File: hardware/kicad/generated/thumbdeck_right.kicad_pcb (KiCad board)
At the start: 2 copper layers, 63 x 107.9 mm, 0 parts

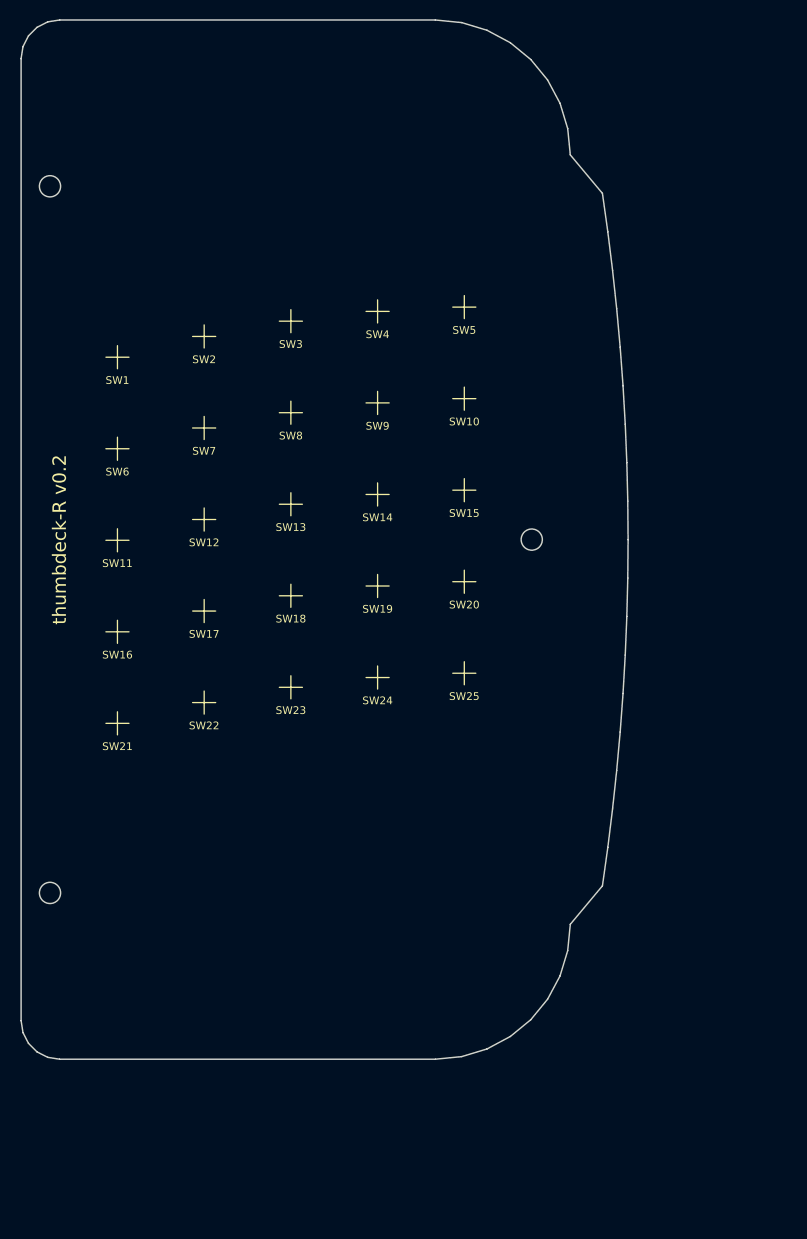
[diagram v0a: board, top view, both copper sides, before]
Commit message: hardware(v0.3): role-based geometry, grader, board gen
- deck.py: right grip = mcu (nice!nano/LiPo/USB-C/bridge), left = passive matrix
  + bridge connector; symmetric outline, mirrored key field
- grade.py: 17 checks incl. F-bridge + F-role; nice!nano pro_micro pin validity;
  single 5x10 transform (dropped split-specific checks)
- gen_kicad/render_fab/matrix_map updated for single controller

Co-Authored-By: Claude Opus 4.8 (1M context) <noreply@anthropic.com>
Claude-Session: https://claude.ai/code/session_01AmPvvwwHX98PjdDnPxhX97
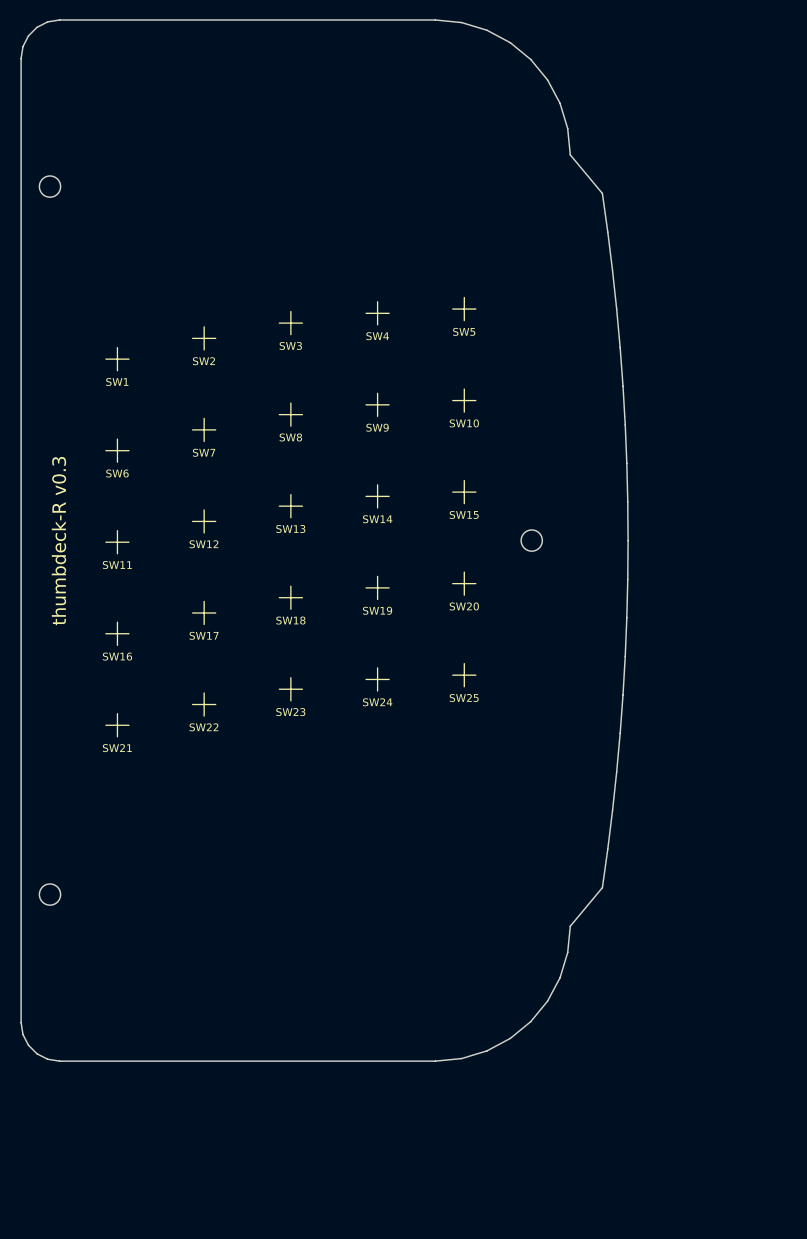
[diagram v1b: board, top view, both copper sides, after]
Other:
- board size 63 x 107.9 mm -> 63 x 108.1 mm
- board text added: "BRIDGE"
- board text added: "thumbdeck-R v0.3"
- board text removed: "thumbdeck-R v0.2"

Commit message: v0.4: encode EE design review into the grade, re-converge to PASS
Turn the professional EE review findings into enforced checks and fix the design
to satisfy them (functional 27/27, visual 9/9, OVERALL PASS).

Geometry/RF:
- nice!nano remounted vertical at top; nRF52840 ANTENNA keep-out overhangs the
  top edge (no copper under RF path), LiPo kept ~90mm away; USB in an access gap
- new hard check F-antenna; F-role now requires antenna on right / passive left

Bridge signal integrity:
- kscan debounce 8ms (F-si-debounce); BOM adds 4.7k row pull-downs, 100-330R
  column series R, TVS, shielded flex (F-si-passives, F-esd-tvs)

Process/plan gates (now graded):
- F-charge (1C vs cell), F-switch-verify (meter pinout), F-review-doc
  (docs/design-review.md + FMEA), F-bringup (current-draw checkpoints),
  F-fab-gates (README gates fab on schematic+ERC+DRC+CI)

Fixes: antenna/controller touching edge tripped float overlap -> 0.6mm gap;
BOM 'series res' substring broke on markdown bold -> looser check.
Bump VERSION v0.3 -> v0.4; regenerate all renders/board/soldermap.

Co-Authored-By: Claude Opus 4.8 (1M context) <noreply@anthropic.com>
Claude-Session: https://claude.ai/code/session_01AmPvvwwHX98PjdDnPxhX97
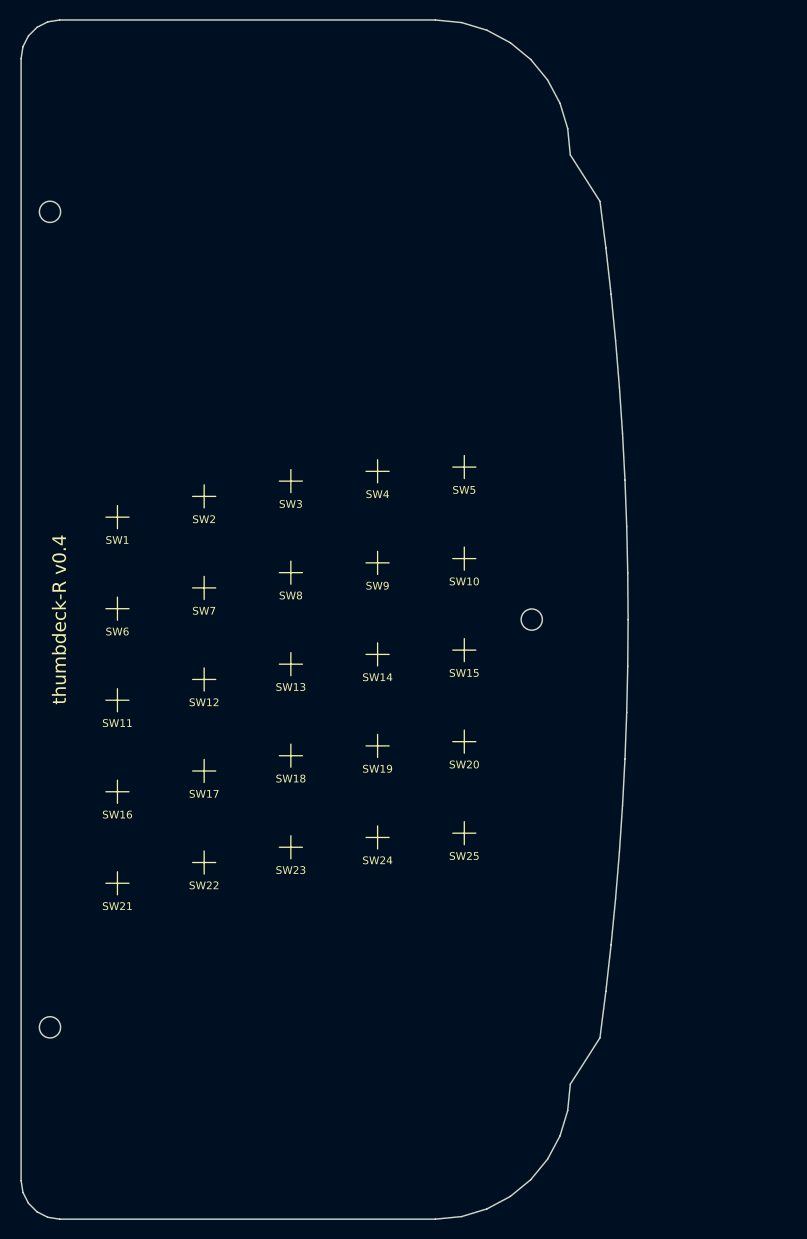
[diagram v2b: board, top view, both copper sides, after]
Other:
- board size 63 x 108.1 mm -> 63 x 124.5 mm
- board text added: "ANTENNA"
- board text added: "thumbdeck-R v0.4"
- board text removed: "thumbdeck-R v0.3"

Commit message: v0.12: snap-dome phone MagSafe deck — module, turnkey PCBA, stackable layer renders
Redesign from v0.4 (50-key nice!nano) to a landscape-phone MagSafe deck:

- Switches: Snaptron 7mm snap domes on a one-piece 3D-printed living-hinge keymat
  (PocketMage-style); footprint extracted to hardware/footprints/. 81 keys (2x 6x6
  grids + D-pad/OK + mouse + PgUp/Dn), digitized from the sketch to
  hardware/layout/keymat.json.
- Form: phone landscape, MagSafe-mounted centre; LiPo in the spine behind the ring;
  two ~70x102mm grips clamped to the outline; PCB-integrated trackpad (Azoteq IQS7211E).
- Electronics (5-lens EE/PD review): one Ebyte E73 nRF52840 module, 9x10 col2row
  matrix with SOD-323 diodes on the back, power front-end (MCP73831/USB-C+CC/ESD),
  vertical JST-GH bridge, ENIG. Layer-correct traces (cols front / rows back / vias),
  PCB meander antenna option.
- Sourcing (JLC vs PCBWay review): JLCPCB single-sided turnkey, ~$150-230/5 sets;
  part swaps + LCSC part numbers in docs/fabrication-sourcing.md.
- Real netlisted KiCad boards via pcbnew (gen_kicad_pcbnew.py) + front/back SVGs.
- 5 stackable layer renders (render_layers.py) + product/fab views; README rewritten.
- Cleanup: old 50-key loop scripts -> hardware/scripts/legacy/; old iters/renders
  -> renders/history/.

Co-Authored-By: Claude Opus 4.8 <noreply@anthropic.com>
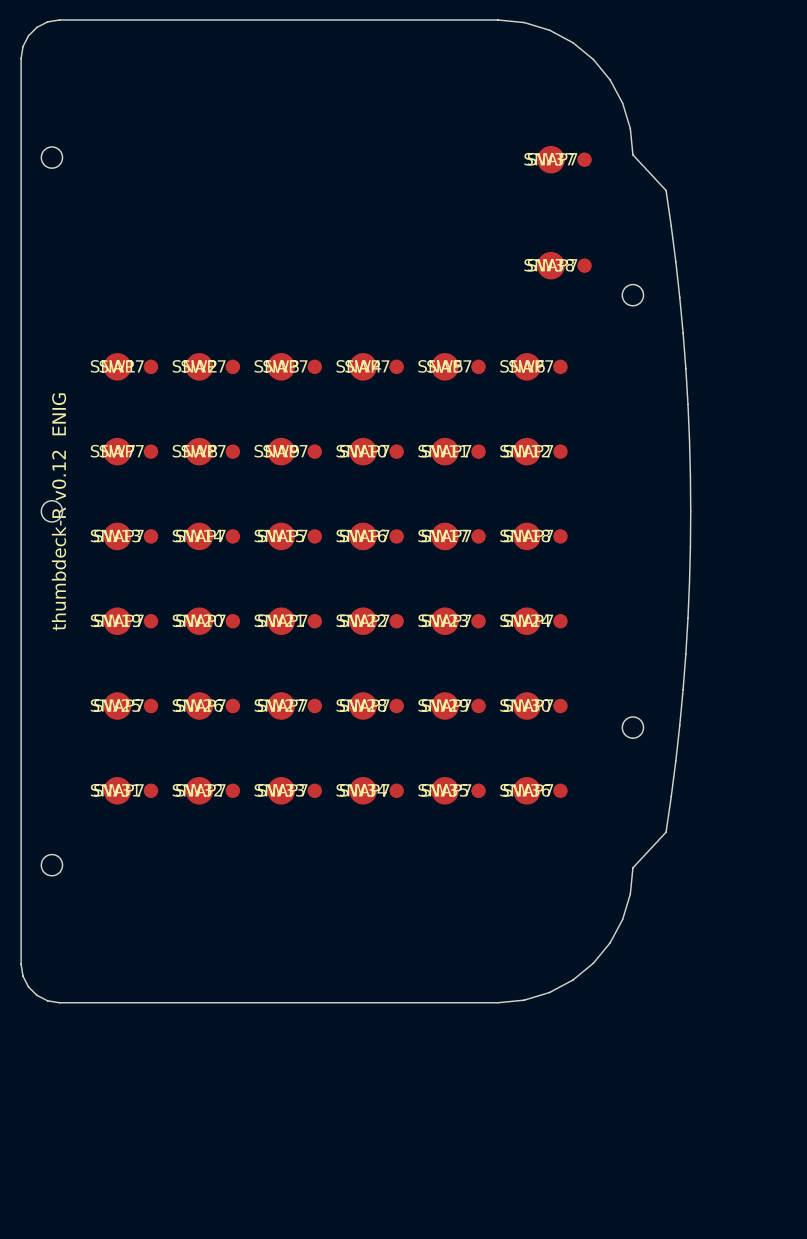
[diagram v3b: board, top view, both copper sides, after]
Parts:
- added D1: 1N4148WS, D_SOD-323, B.Cu at (10.0, 35.8)
- added D10: 1N4148WS, D_SOD-323, B.Cu at (35.5, 44.6)
- added D11: 1N4148WS, D_SOD-323, B.Cu at (44.0, 44.6)
- added D12: 1N4148WS, D_SOD-323, B.Cu at (52.5, 44.6)
- added D13: 1N4148WS, D_SOD-323, B.Cu at (10.0, 53.4)
- added D14: 1N4148WS, D_SOD-323, B.Cu at (18.5, 53.4)
- added D15: 1N4148WS, D_SOD-323, B.Cu at (27.0, 53.4)
- added D16: 1N4148WS, D_SOD-323, B.Cu at (35.5, 53.4)
- added D17: 1N4148WS, D_SOD-323, B.Cu at (44.0, 53.4)
- added D18: 1N4148WS, D_SOD-323, B.Cu at (52.5, 53.4)
- added D19: 1N4148WS, D_SOD-323, B.Cu at (10.0, 62.2)
- added D2: 1N4148WS, D_SOD-323, B.Cu at (18.5, 35.8)
- added D20: 1N4148WS, D_SOD-323, B.Cu at (18.5, 62.2)
- added D21: 1N4148WS, D_SOD-323, B.Cu at (27.0, 62.2)
- added D22: 1N4148WS, D_SOD-323, B.Cu at (35.5, 62.2)
- added D23: 1N4148WS, D_SOD-323, B.Cu at (44.0, 62.2)
- added D24: 1N4148WS, D_SOD-323, B.Cu at (52.5, 62.2)
- added D25: 1N4148WS, D_SOD-323, B.Cu at (10.0, 71.0)
- added D26: 1N4148WS, D_SOD-323, B.Cu at (18.5, 71.0)
- added D27: 1N4148WS, D_SOD-323, B.Cu at (27.0, 71.0)
- added D28: 1N4148WS, D_SOD-323, B.Cu at (35.5, 71.0)
- added D29: 1N4148WS, D_SOD-323, B.Cu at (44.0, 71.0)
- added D3: 1N4148WS, D_SOD-323, B.Cu at (27.0, 35.8)
- added D30: 1N4148WS, D_SOD-323, B.Cu at (52.5, 71.0)
- added D31: 1N4148WS, D_SOD-323, B.Cu at (10.0, 79.8)
- added D32: 1N4148WS, D_SOD-323, B.Cu at (18.5, 79.8)
- added D33: 1N4148WS, D_SOD-323, B.Cu at (27.0, 79.8)
- added D34: 1N4148WS, D_SOD-323, B.Cu at (35.5, 79.8)
- added D35: 1N4148WS, D_SOD-323, B.Cu at (44.0, 79.8)
- added D36: 1N4148WS, D_SOD-323, B.Cu at (52.5, 79.8)
- added D37: 1N4148WS, D_SOD-323, B.Cu at (55.0, 14.3)
- added D38: 1N4148WS, D_SOD-323, B.Cu at (55.0, 25.3)
- added D4: 1N4148WS, D_SOD-323, B.Cu at (35.5, 35.8)
- added D5: 1N4148WS, D_SOD-323, B.Cu at (44.0, 35.8)
- added D6: 1N4148WS, D_SOD-323, B.Cu at (52.5, 35.8)
- added D7: 1N4148WS, D_SOD-323, B.Cu at (10.0, 44.6)
- added D8: 1N4148WS, D_SOD-323, B.Cu at (18.5, 44.6)
- added D9: 1N4148WS, D_SOD-323, B.Cu at (27.0, 44.6)
- added SW1: SNAP7, , F.Cu at (10.0, 36.0)
- added SW10: SNAP7, , F.Cu at (35.5, 44.8)
- added SW11: SNAP7, , F.Cu at (44.0, 44.8)
- added SW12: SNAP7, , F.Cu at (52.5, 44.8)
- added SW13: SNAP7, , F.Cu at (10.0, 53.6)
- added SW14: SNAP7, , F.Cu at (18.5, 53.6)
- added SW15: SNAP7, , F.Cu at (27.0, 53.6)
- added SW16: SNAP7, , F.Cu at (35.5, 53.6)
- added SW17: SNAP7, , F.Cu at (44.0, 53.6)
- added SW18: SNAP7, , F.Cu at (52.5, 53.6)
- added SW19: SNAP7, , F.Cu at (10.0, 62.4)
- added SW2: SNAP7, , F.Cu at (18.5, 36.0)
- added SW20: SNAP7, , F.Cu at (18.5, 62.4)
- added SW21: SNAP7, , F.Cu at (27.0, 62.4)
- added SW22: SNAP7, , F.Cu at (35.5, 62.4)
- added SW23: SNAP7, , F.Cu at (44.0, 62.4)
- added SW24: SNAP7, , F.Cu at (52.5, 62.4)
- added SW25: SNAP7, , F.Cu at (10.0, 71.2)
- added SW26: SNAP7, , F.Cu at (18.5, 71.2)
- added SW27: SNAP7, , F.Cu at (27.0, 71.2)
- added SW28: SNAP7, , F.Cu at (35.5, 71.2)
- added SW29: SNAP7, , F.Cu at (44.0, 71.2)
- added SW3: SNAP7, , F.Cu at (27.0, 36.0)
- added SW30: SNAP7, , F.Cu at (52.5, 71.2)
- added SW31: SNAP7, , F.Cu at (10.0, 80.0)
- added SW32: SNAP7, , F.Cu at (18.5, 80.0)
- added SW33: SNAP7, , F.Cu at (27.0, 80.0)
- added SW34: SNAP7, , F.Cu at (35.5, 80.0)
- added SW35: SNAP7, , F.Cu at (44.0, 80.0)
- added SW36: SNAP7, , F.Cu at (52.5, 80.0)
- added SW37: SNAP7, , F.Cu at (55.0, 14.5)
- added SW38: SNAP7, , F.Cu at (55.0, 25.5)
- added SW4: SNAP7, , F.Cu at (35.5, 36.0)
- added SW5: SNAP7, , F.Cu at (44.0, 36.0)
- added SW6: SNAP7, , F.Cu at (52.5, 36.0)
- added SW7: SNAP7, , F.Cu at (10.0, 44.8)
- added SW8: SNAP7, , F.Cu at (18.5, 44.8)
- added SW9: SNAP7, , F.Cu at (27.0, 44.8)
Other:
- board size 63 x 124.5 mm -> 69.5 x 102 mm
- board text added: "CHARGER"
- board text added: "ROUTING + MODULE/CONN FOOTPRINTS = NEXT GATE"
- board text added: "TRACKPAD-TPS43-OPT"
- board text added: "USB_C"
- board text added: "thumbdeck-R v0.12 ENIG"
- board text removed: "D1"
- board text removed: "D10"
- board text removed: "D11"
- board text removed: "D12"
- board text removed: "D13"
- board text removed: "D14"
- board text removed: "D15"
- board text removed: "D16"
- board text removed: "D17"
- board text removed: "D18"
- board text removed: "D19"
- board text removed: "D2"
- board text removed: "D20"
- board text removed: "D21"
- board text removed: "D22"
- board text removed: "D23"
- board text removed: "D24"
- board text removed: "D25"
- board text removed: "D3"
- board text removed: "D4"
- board text removed: "D5"
- board text removed: "D6"
- board text removed: "D7"
- board text removed: "D8"
- board text removed: "D9"
- board text removed: "LIPO"
- board text removed: "SW1"
- board text removed: "SW10"
- board text removed: "SW11"
- board text removed: "SW12"
- board text removed: "SW13"
- board text removed: "SW14"
- board text removed: "SW15"
- board text removed: "SW16"
- board text removed: "SW17"
- board text removed: "SW18"
- board text removed: "SW19"
- board text removed: "SW2"
- board text removed: "SW20"
- board text removed: "SW21"
- board text removed: "SW22"
- board text removed: "SW23"
- board text removed: "SW24"
- board text removed: "SW25"
- board text removed: "SW3"
- board text removed: "SW4"
- board text removed: "SW5"
- board text removed: "SW6"
- board text removed: "SW7"
- board text removed: "SW8"
- board text removed: "SW9"
- board text removed: "SWITCH FOOTPRINT PROVISIONAL - VERIFY vs DATASHEET"
- board text removed: "USB-C"
- board text removed: "thumbdeck-R v0.4"

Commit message: v0.13: printable pitch, 2u space bar, cluster/screw/keymat fixes
Feedback fixes (all verified: no overlaps, nothing off-board, no screw in a keep-out):
- #5 DFM: pitch 8.5/8.8 -> 9.5mm so the inter-key wall is ~1.5mm (printable in PETG;
  0.5mm was not). Matches the i8+ pitch. Grips -> 74.5x109.5mm, 79 keys.
- #4: drop MENU keys, shift bottom row, add a double-wide 2u space bar per side
  (dome stays single under the wide keycap; keys carry a 'w' width in units).
- #2: D-pad no longer overlaps the F-row (upper zone sized to clear the cluster,
  clusters centred instead of offset down).
- #1: bottom-inner mount hole moved below the vertical JST-GH bridge connector.
- #3: keymat now ties every cluster keycap into the living-hinge web.

Co-Authored-By: Claude Opus 4.8 <noreply@anthropic.com>
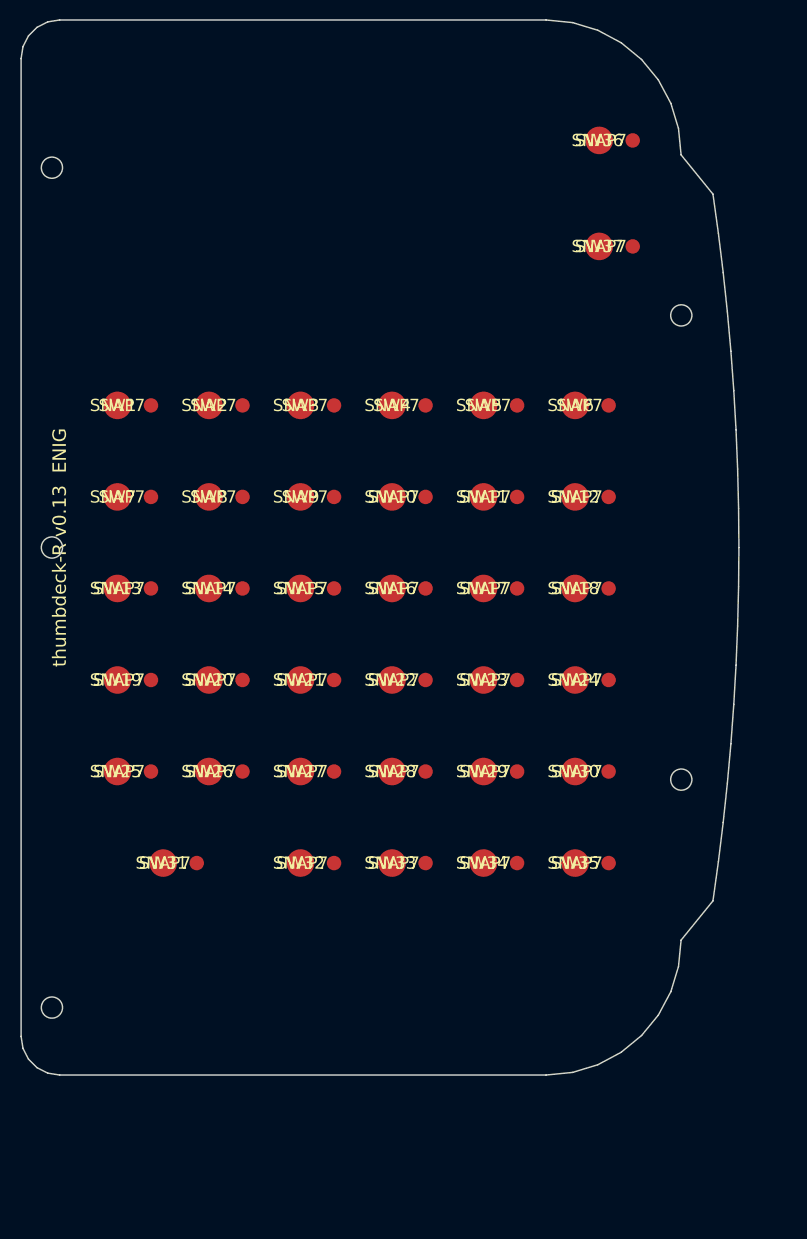
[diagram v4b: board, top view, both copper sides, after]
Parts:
- removed D38: 1N4148WS, D_SOD-323
- removed SW38: SNAP7, 
- moved D36 67.9 mm to (60.0, 12.3)
- moved SW36 67.9 mm to (60.0, 12.5)
- moved D35 15.4 mm to (57.5, 87.3)
- moved SW35 15.4 mm to (57.5, 87.5)
- moved D34 14.6 mm to (48.0, 87.3)
- moved SW34 14.6 mm to (48.0, 87.5)
- moved D33 13.7 mm to (38.5, 87.3)
- moved SW33 13.7 mm to (38.5, 87.5)
- moved D32 12.9 mm to (29.0, 87.3)
- moved SW32 12.9 mm to (29.0, 87.5)
- moved D37 10.3 mm to (60.0, 23.3)
- moved SW37 10.3 mm to (60.0, 23.5)
- moved D31 8.88 mm to (14.8, 87.3)
- moved SW31 8.88 mm to (14.8, 87.5)
- moved D30 8.44 mm to (57.5, 77.8)
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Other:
- board size 69.5 x 102 mm -> 74.5 x 109.5 mm
- board text added: "thumbdeck-R v0.13 ENIG"
- board text removed: "thumbdeck-R v0.12 ENIG"
